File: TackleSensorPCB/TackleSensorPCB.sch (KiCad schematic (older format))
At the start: 24 parts, among them J1 PJ-037A, J2 Conn_01x03_Male, J3 Conn_01x03_Male, J4 Conn_01x07_Male, Q1 2N7002, Q2 2N7002, SW1 SW_DPST_x2, U1 TPS62172DSG, U2 MSP430FR2433IRGER, U3 MMA8452QR1

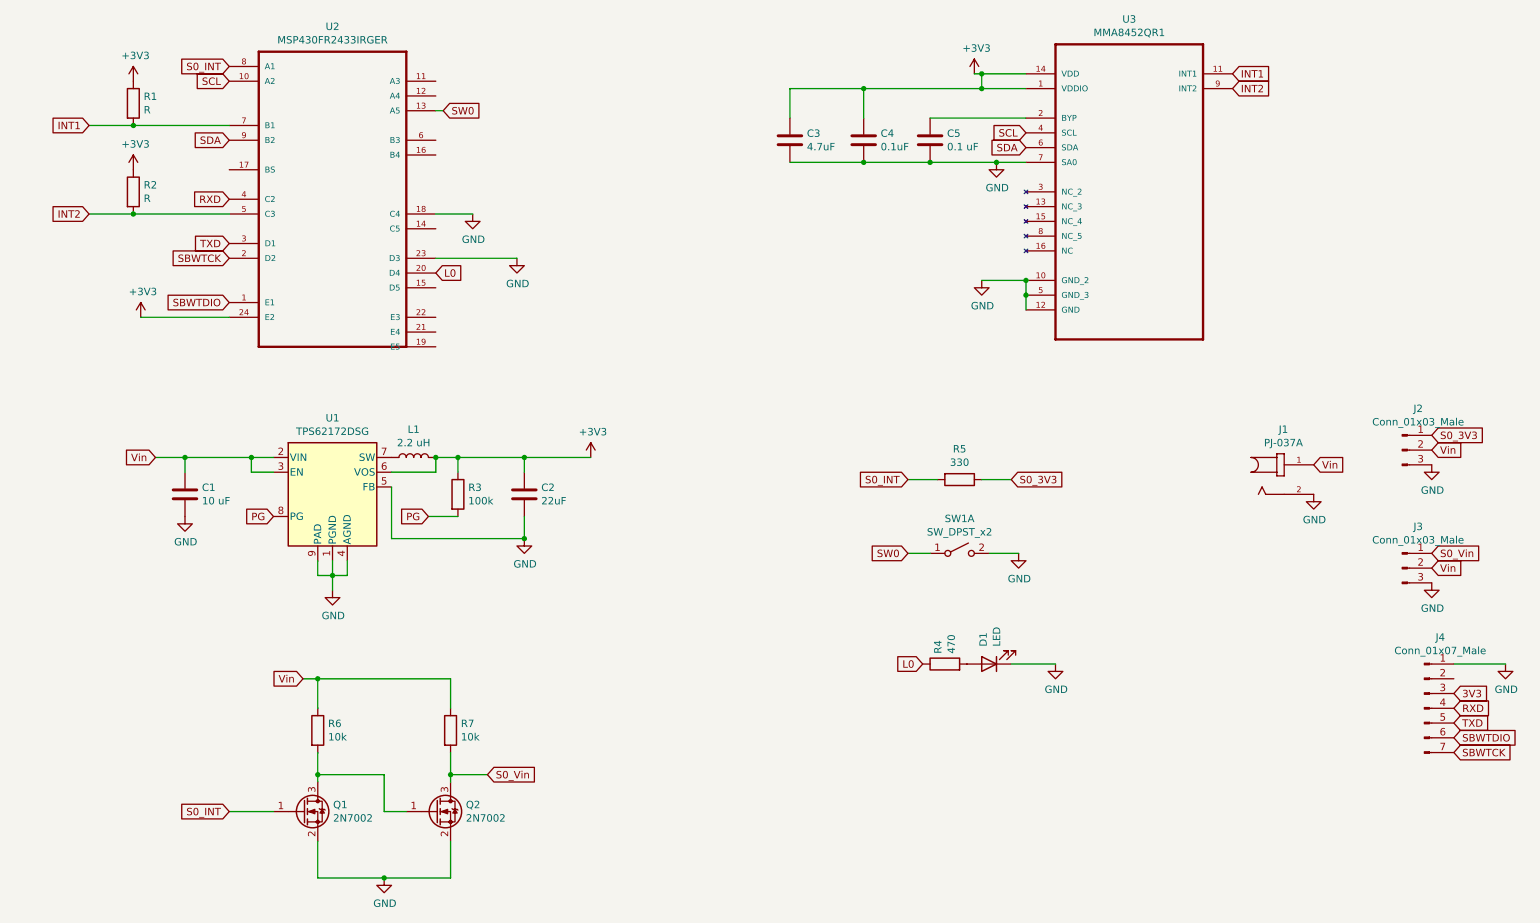
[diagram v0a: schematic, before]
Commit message: Added Fuse
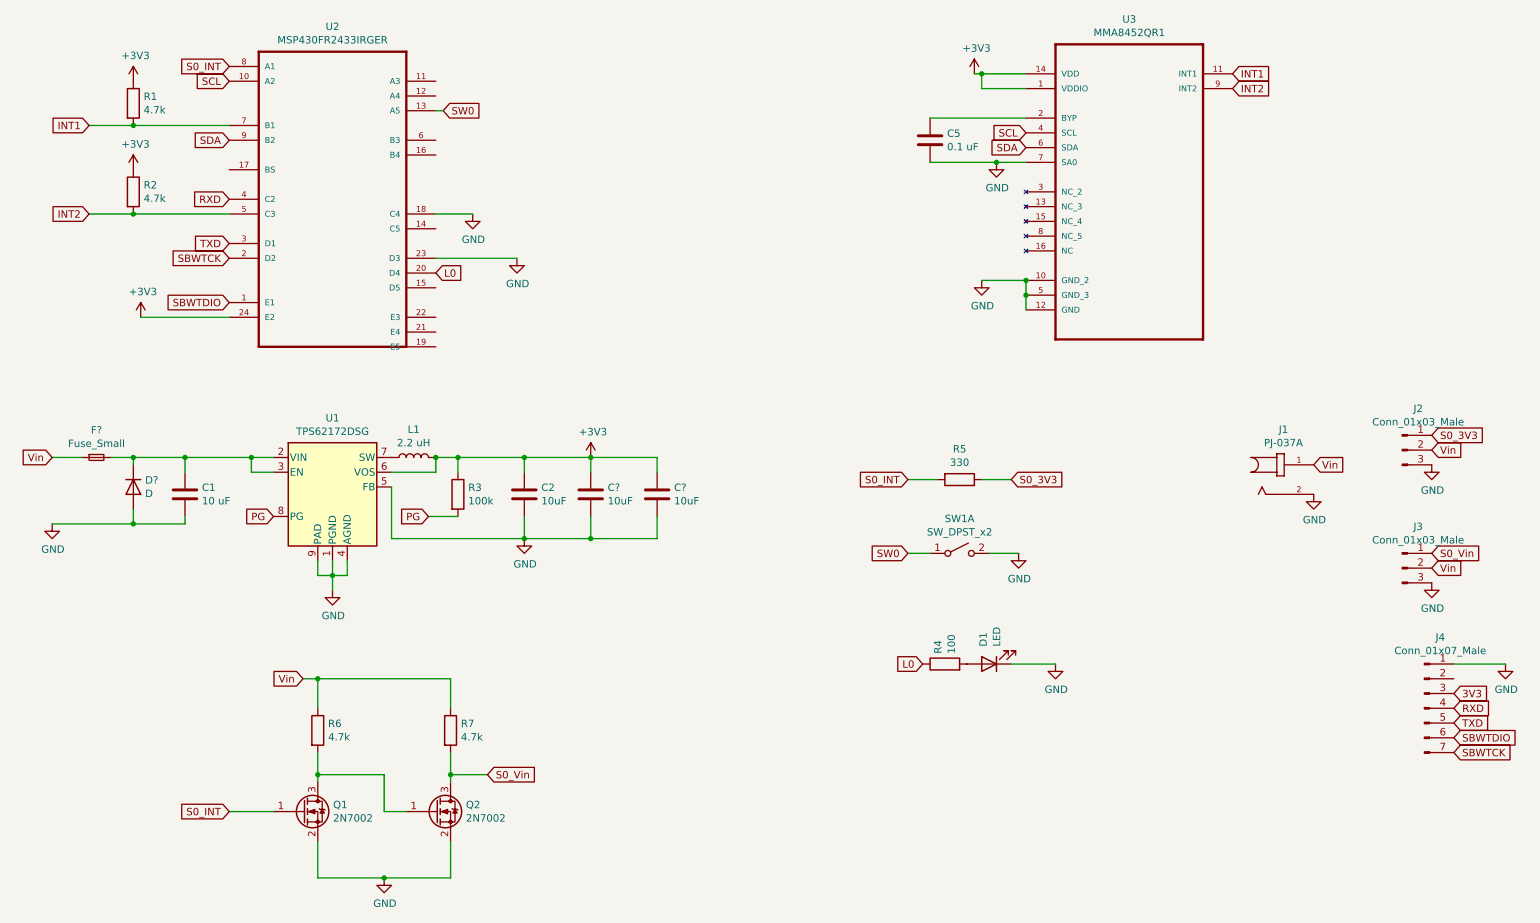
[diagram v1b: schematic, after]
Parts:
- removed C3: 4.7uF, symbol Device:C
- removed C4: 0.1uF, symbol Device:C
- added C? (x2): 10uF, symbol Device:C
- added D?: D, symbol Device:D
- added F?: Fuse_Small, symbol Device:Fuse_Small
- C2: value 22uF -> 10uF
- R1, R2: value R -> 4.7k
- R4: value 470 -> 100
- R6, R7: value 10k -> 4.7k
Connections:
- net +3V3: now also C?.1, C?.1
- net GND: now also C?.2, C?.2, D?.2 (A)
- net Vin: now also F?.1; no longer C1.1, U1.2 (VIN), U1.3 (EN)
- new net: C1.1, D?.1 (K), F?.2, U1.2 (VIN), U1.3 (EN)
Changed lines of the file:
@@
 	1900 4200 1900 4300
 Connection ~ 2350 4200
-Text GLabel 1700 4200 0    50   Input ~ 0
+Text GLabel 1000 4200 0    50   Input ~ 0
 Vin
-Wire Wire Line
-	1700 4200 1900 4200
 Connection ~ 1900 4200
 $Comp
 L power:GND #PWR04
 U 1 1 5F833346
-P 1900 4600
-F 0 "#PWR04" H 1900 4350 50  0001 C CNN
-F 1 "GND" H 1905 4427 50  0000 C CNN
-F 2 "" H 1900 4600 50  0001 C CNN
-F 3 "" H 1900 4600 50  0001 C CNN
-	1    1900 4600
+P 1000 4650
+F 0 "#PWR04" H 1000 4400 50  0001 C CNN
+F 1 "GND" H 1005 4477 50  0000 C CNN
+F 2 "" H 1000 4650 50  0001 C CNN
+F 3 "" H 1000 4650 50  0001 C CNN
+	1    1000 4650
 	1    0    0    -1
 $EndComp
@@
 Wire Wire Line
 	3550 4600 3750 4600
-Wire Wire Line
-	3750 4200 4200 4200
-Wire Wire Line
-	4200 4200 4200 4300
 Connection ~ 3750 4200
 Wire Wire Line
 	3300 4750 3300 4400
-Wire Wire Line
-	4200 4200 4650 4200
-Connection ~ 4200 4200
 $Comp
 L power:+3V3 #PWR08
@@
 P 1550 2400
 F 0 "R2" H 1620 2446 50  0000 L CNN
-F 1 "R" H 1620 2355 50  0000 L CNN
+F 1 "4.7k" H 1620 2355 50  0000 L CNN
 F 2 "" V 1480 2400 50  0001 C CNN
 F 3 "~" H 1550 2400 50  0001 C CNN
@@
 P 1550 1800
 F 0 "R1" H 1620 1846 50  0000 L CNN
-F 1 "R" H 1620 1755 50  0000 L CNN
+F 1 "4.7k" H 1620 1755 50  0000 L CNN
 F 2 "" V 1480 1800 50  0001 C CNN
 F 3 "~" H 1550 1800 50  0001 C CNN
@@
 $EndComp
 $Comp
-L Device:C C4
-U 1 1 5F840811
-P 6500 2050
-F 0 "C4" H 6615 2096 50  0000 L CNN
-F 1 "0.1uF" H 6615 2005 50  0000 L CNN
-F 2 "" H 6538 1900 50  0001 C CNN
-F 3 "~" H 6500 2050 50  0001 C CNN
-	1    6500 2050
-	1    0    0    -1
-$EndComp
-$Comp
 L Device:C C5
 U 1 1 5F841354
@@
 Connection ~ 7400 2200
 Wire Wire Line
-	6500 2200 6950 2200
-Wire Wire Line
-	6500 1900 6500 1700
-Wire Wire Line
-	6500 1700 7300 1700
-Connection ~ 7300 1700
-$Comp
-L Device:C C3
-U 1 1 5F847A63
-P 6000 2050
-F 0 "C3" H 6115 2096 50  0000 L CNN
-F 1 "4.7uF" H 6115 2005 50  0000 L CNN
-F 2 "" H 6038 1900 50  0001 C CNN
-F 3 "~" H 6000 2050 50  0001 C CNN
-	1    6000 2050
-	1    0    0    -1
-$EndComp
-Wire Wire Line
-	6000 2200 6500 2200
-Connection ~ 6500 2200
-Wire Wire Line
-	6000 1900 6000 1700
-Wire Wire Line
-	6000 1700 6500 1700
-Connection ~ 6500 1700
-Wire Wire Line
 	7600 3100 7600 3000
 Wire Wire Line
@@
 Text GLabel 7600 2100 0    50   Input ~ 0
 SDA
-Connection ~ 6950 2200
 Wire Wire Line
 	6950 2200 7400 2200
@@
 P 2800 6050
 F 0 "R6" H 2870 6096 50  0000 L CNN
-F 1 "10k" H 2870 6005 50  0000 L CNN
+F 1 "4.7k" H 2870 6005 50  0000 L CNN
 F 2 "" V 2730 6050 50  0001 C CNN
 F 3 "~" H 2800 6050 50  0001 C CNN
@@
 P 3700 6050
 F 0 "R7" H 3770 6096 50  0000 L CNN
-F 1 "10k" H 3770 6005 50  0000 L CNN
+F 1 "4.7k" H 3770 6005 50  0000 L CNN
 F 2 "" V 3630 6050 50  0001 C CNN
 F 3 "~" H 3700 6050 50  0001 C CNN
@@
 Wire Wire Line
 	4200 4600 4200 4750
-$Comp
-L Device:C C2
-U 1 1 5F836FD6
-P 4200 4450
-F 0 "C2" H 4315 4496 50  0000 L CNN
-F 1 "22uF" H 4315 4405 50  0000 L CNN
-F 2 "" H 4238 4300 50  0001 C CNN
-F 3 "~" H 4200 4450 50  0001 C CNN
-	1    4200 4450
-	1    0    0    -1
-$EndComp
 $Comp
 L power:GND #PWR?
@@
 P 7050 5600
 F 0 "R4" H 7120 5646 50  0000 L CNN
-F 1 "470" H 7120 5555 50  0000 L CNN
+F 1 "100" H 7120 5555 50  0000 L CNN
 F 2 "" V 6980 5600 50  0001 C CNN
 F 3 "~" H 7050 5600 50  0001 C CNN
@@
 	0    -1   -1   0
 $EndComp
+Connection ~ 4200 4200
+Wire Wire Line
+	4200 4200 4650 4200
+Wire Wire Line
+	3750 4200 4200 4200
+$Comp
+L Device:C C2
+U 1 1 5F836FD6
+P 4200 4450
+F 0 "C2" H 4315 4496 50  0000 L CNN
+F 1 "10uF" H 4315 4405 50  0000 L CNN
+F 2 "" H 4238 4300 50  0001 C CNN
+F 3 "~" H 4200 4450 50  0001 C CNN
+	1    4200 4450
+	1    0    0    -1
+$EndComp
+Wire Wire Line
+	4200 4200 4200 4300
+$Comp
+L Device:C C?
+U 1 1 5F841E73
+P 4650 4450
+F 0 "C?" H 4765 4496 50  0000 L CNN
+F 1 "10uF" H 4765 4405 50  0000 L CNN
+F 2 "" H 4688 4300 50  0001 C CNN
+F 3 "~" H 4650 4450 50  0001 C CNN
+	1    4650 4450
+	1    0    0    -1
+$EndComp
+Wire Wire Line
+	4650 4200 4650 4300
+$Comp
+L Device:C C?
+U 1 1 5F8433F9
+P 5100 4450
+F 0 "C?" H 5215 4496 50  0000 L CNN
+F 1 "10uF" H 5215 4405 50  0000 L CNN
+F 2 "" H 5138 4300 50  0001 C CNN
+F 3 "~" H 5100 4450 50  0001 C CNN
+	1    5100 4450
+	1    0    0    -1
+$EndComp
+Wire Wire Line
+	5100 4200 5100 4300
+Wire Wire Line
+	4200 4750 4650 4750
+Wire Wire Line
+	4650 4750 4650 4600
+Wire Wire Line
+	4650 4750 5100 4750
+Wire Wire Line
+	5100 4750 5100 4600
+Connection ~ 4650 4750
+Wire Wire Line
+	4650 4200 5100 4200
+Connection ~ 4650 4200
+$Comp
+L Device:Fuse_Small F?
+U 1 1 5F8414C0
+P 1300 4200
+F 0 "F?" H 1300 4385 50  0000 C CNN
+F 1 "Fuse_Small" H 1300 4294 50  0000 C CNN
+F 2 "" H 1300 4200 50  0001 C CNN
+F 3 "~" H 1300 4200 50  0001 C CNN
+	1    1300 4200
+	1    0    0    -1
+$EndComp
+Wire Wire Line
+	1000 4200 1200 4200
+Wire Wire Line
+	1400 4200 1550 4200
+Wire Wire Line
+	1000 4650 1550 4650
+Wire Wire Line
+	1900 4650 1900 4600
+$Comp
+L Device:D D?
+U 1 1 5F849611
+P 1550 4400
+F 0 "D?" V 1504 4480 50  0000 L CNN
+F 1 "D" V 1595 4480 50  0000 L CNN
+F 2 "" H 1550 4400 50  0001 C CNN
+F 3 "~" H 1550 4400 50  0001 C CNN
+	1    1550 4400
+	0    1    1    0
+$EndComp
+Wire Wire Line
+	1550 4250 1550 4200
+Connection ~ 1550 4200
+Wire Wire Line
+	1550 4200 1900 4200
+Wire Wire Line
+	1550 4550 1550 4650
+Connection ~ 1550 4650
+Wire Wire Line
+	1550 4650 1900 4650
 $EndSCHEMATC
